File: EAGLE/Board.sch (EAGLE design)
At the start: 168 parts, among them J1 JUMPER_SOLDER_1X2, J10 JUMPER_SOLDER_1X2, J11 JUMPER_SOLDER_1X2, J12 KF301-2P, J2 JUMPER_SOLDER_1X2, J3 JUMPER_SOLDER_1X2, J4 JUMPER_SOLDER_1X2, J5 JUMPER_SOLDER_1X2, J6 JUMPER_SOLDER_1X2, J8 KF301-2P, J9 JUMPER_SOLDER_1X2, Q1 500mA/300V, Q2 500mA/300V, Q3 FDN337N, U1 SN74HC04PW, U2 ESP32-WROOM-32, U3 CH340C, U4 AMS1117, U6 PCA9635PW, U7 SN74HC04PW, U8 SN74HC04PW, U9 LTC1694IS5#TRPBF, X1 JST-XH-04-PIN-LONG-PAD, X2 JST-XH-04-PIN-LONG-PAD, X3 JST-XH-02-PIN-LONG-PAD

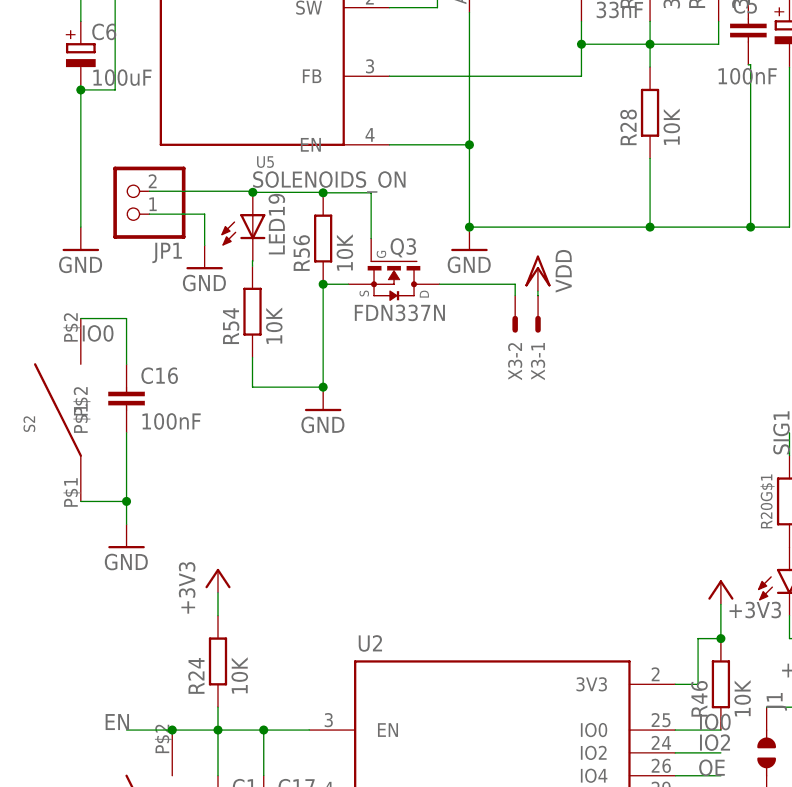
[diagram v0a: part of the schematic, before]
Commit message: Update EAGLE files to latest version
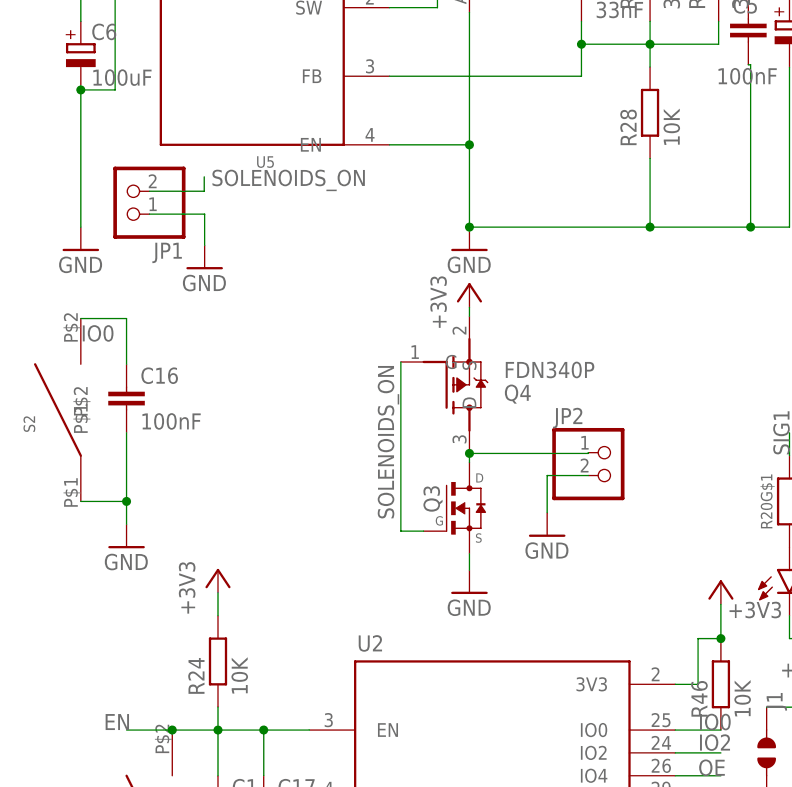
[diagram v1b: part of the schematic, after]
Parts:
- removed LED19: (no value), dp_devices:LED-0603
- removed R54, R56: 10K, rcl:R-EU_R0603
- removed X3: JST-XH-02-PIN-LONG-PAD, Rembrandt Electronics - JST XH Connectors v1-0:JST-XH-02-PIN-LONG-PAD
- added JP2: (no value), pinhead:PINHD-1X2
- added Q4: FDN340P, FDN340P:FDN340P
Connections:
- removed net N$83: LED19.C, R54.2
- net +3V3: now also Q4.S
- net GND: now also JP2.2; no longer R54.1, R56.1
- net N$37: now also JP2.1, Q4.D; no longer X3-2.S
- net SOLENOIDS_ON: now also Q4.G; no longer LED19.A, R56.2
- net VDD: no longer X3-1.S
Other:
- moved on the sheet: Q3
